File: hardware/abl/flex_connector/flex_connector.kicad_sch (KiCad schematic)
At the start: 2 parts, among them J1 Conn_01x20_Pin, J2 Conn_01x20_Pin

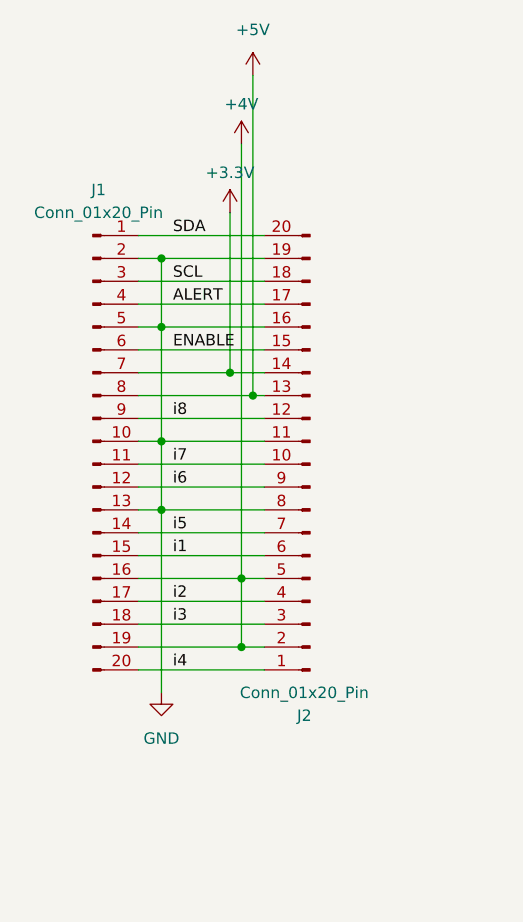
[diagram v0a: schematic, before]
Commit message: Rename files, names and labels to be more consistent. Add READMEs for connectors and extend some other READMEs.
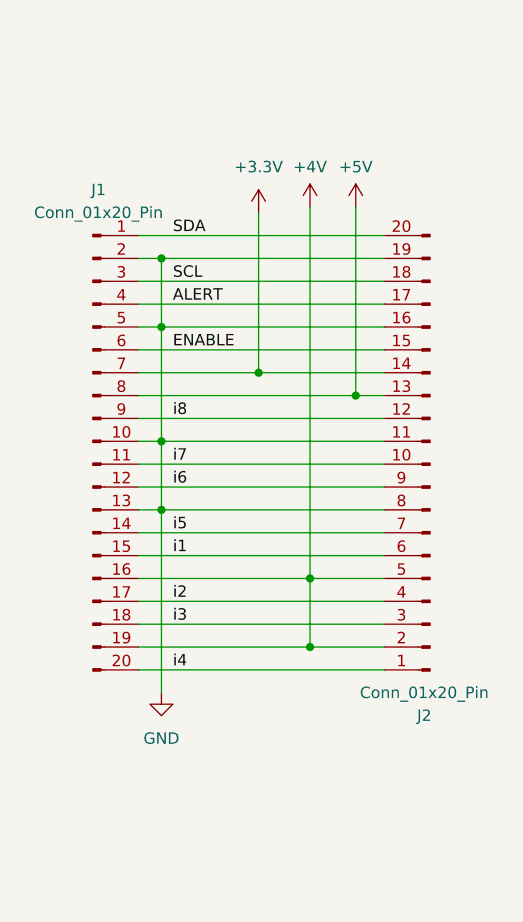
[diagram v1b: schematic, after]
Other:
- title: (none) -> besteLampe! ABL Flex Connector
- moved on the sheet: J2

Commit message: Add current renderings to all ABL PCBs.
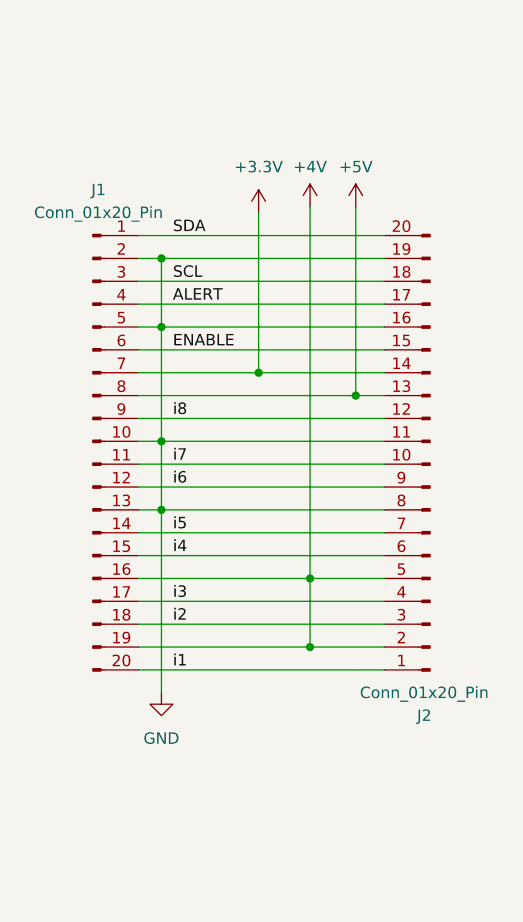
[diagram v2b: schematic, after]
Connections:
- net i1: now also J1.20 (Pin_20), J2.1 (Pin_1); no longer J1.15 (Pin_15), J2.6 (Pin_6)
- net i2: now also J1.18 (Pin_18), J2.3 (Pin_3); no longer J1.17 (Pin_17), J2.4 (Pin_4)
- net i3: now also J1.17 (Pin_17), J2.4 (Pin_4); no longer J1.18 (Pin_18), J2.3 (Pin_3)
- net i4: now also J1.15 (Pin_15), J2.6 (Pin_6); no longer J1.20 (Pin_20), J2.1 (Pin_1)
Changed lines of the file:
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@@
 	)
 	(label "i2"
-		(at 58.42 95.25 0)
+		(at 58.42 97.79 0)
 		(fields_autoplaced yes)
 		(effects
@@
 	)
 	(label "i3"
-		(at 58.42 97.79 0)
+		(at 58.42 95.25 0)
 		(fields_autoplaced yes)
 		(effects
@@
 	)
 	(label "i4"
-		(at 58.42 102.87 0)
+		(at 58.42 90.17 0)
 		(fields_autoplaced yes)
 		(effects
@@
 	)
 	(label "i1"
-		(at 58.42 90.17 0)
+		(at 58.42 102.87 0)
 		(fields_autoplaced yes)
 		(effects
@@
 		(on_board yes)
 		(dnp no)
-		(fields_autoplaced yes)
 		(property "Reference" "J1"
 			(at 50.165 49.53 0)

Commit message: Many small adjustments for the next production run.
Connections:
- net +5V is gone; now on net +4V: J1.8 (Pin_8), J2.13 (Pin_13)
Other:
- note added: "Pin numbering of this schematics / symbols contradicts that of the rigid PCBs, but the result should be all right."
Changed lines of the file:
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@@
 	(title_block
 		(title "besteLampe! ABL Flex Connector")
-		(date "2024-10-01")
-		(rev "1.0")
+		(date "2024-11-26")
+		(rev "1.1")
 		(comment 1 "See  https://lenaschimmel.de/besteLampe! for the source and more information")
 		(comment 2 "This source describes Open Hardware and is licensed under the CERN-OHL-S v2.")
@@
 	)
 	(junction
+		(at 73.66 46.355)
+		(diameter 0)
+		(color 0 0 0 0)
+	)
+	(junction
+		(at 78.74 46.355)
+		(diameter 0)
+		(color 0 0 0 0)
+	)
+	(junction
 		(at 67.945 69.85)
 		(diameter 0)
@@
 	(wire
 		(pts
-			(xy 78.74 51.435) (xy 78.74 72.39)
+			(xy 78.74 43.18) (xy 78.74 46.355)
+		)
+		(stroke
+			(width 0)
+			(type default)
+		)
+	)
+	(wire
+		(pts
+			(xy 78.74 46.355) (xy 78.74 72.39)
 		)
 		(stroke
@@
 	(wire
 		(pts
-			(xy 73.66 51.435) (xy 73.66 92.71)
+			(xy 73.66 43.18) (xy 73.66 46.355)
 		)
 		(stroke
@@
 	(wire
 		(pts
+			(xy 73.66 46.355) (xy 73.66 92.71)
+		)
+		(stroke
+			(width 0)
+			(type default)
+		)
+	)
+	(wire
+		(pts
 			(xy 67.945 69.85) (xy 81.915 69.85)
 		)
@@
 	(wire
 		(pts
+			(xy 73.66 46.355) (xy 78.74 46.355)
+		)
+		(stroke
+			(width 0)
+			(type default)
+		)
+	)
+	(wire
+		(pts
 			(xy 54.61 92.71) (xy 73.66 92.71)
 		)
@@
 			(width 0)
 			(type default)
+		)
+	)
+	(text "Pin numbering of this schematics / symbols\ncontradicts that of the rigid PCBs, but \nthe result should be all right."
+		(exclude_from_sim no)
+		(at 68.58 125.73 0)
+		(effects
+			(font
+				(size 1.27 1.27)
+			)
 		)
 	)
@@
 	(symbol
 		(lib_id "power:+5V")
-		(at 78.74 51.435 0)
+		(at 78.74 43.18 0)
 		(unit 1)
 		(exclude_from_sim no)
@@
 		(dnp no)
 		(property "Reference" "#PWR09"
-			(at 78.74 55.245 0)
+			(at 78.74 46.99 0)
 			(effects
 				(font
@@
 		)
 		(property "Value" "+5V"
-			(at 78.74 46.99 0)
+			(at 78.74 38.735 0)
 			(effects
 				(font
@@
 		)
 		(property "Footprint" ""
-			(at 78.74 51.435 0)
+			(at 78.74 43.18 0)
 			(effects
 				(font
@@
 		)
 		(property "Datasheet" ""
-			(at 78.74 51.435 0)
+			(at 78.74 43.18 0)
 			(effects
 				(font
@@
 		)
 		(property "Description" "Power symbol creates a global label with name \"+5V\""
-			(at 78.74 51.435 0)
+			(at 78.74 43.18 0)
 			(effects
 				(font
@@
 	(symbol
 		(lib_id "power:+4V")
-		(at 73.66 51.435 0)
+		(at 73.66 43.18 0)
 		(unit 1)
 		(exclude_from_sim no)
@@
 		(fields_autoplaced yes)
 		(property "Reference" "#PWR010"
-			(at 73.66 55.245 0)
+			(at 73.66 46.99 0)
 			(effects
 				(font
@@
 		)
 		(property "Value" "+4V"
-			(at 73.66 46.99 0)
+			(at 73.66 38.735 0)
 			(effects
 				(font
@@
 		)
 		(property "Footprint" ""
-			(at 73.66 51.435 0)
+			(at 73.66 43.18 0)
 			(effects
 				(font
@@
 		)
 		(property "Datasheet" ""
-			(at 73.66 51.435 0)
+			(at 73.66 43.18 0)
 			(effects
 				(font
@@
 		)
 		(property "Description" "Power symbol creates a global label with name \"+4V\""
-			(at 73.66 51.435 0)
-			(effects
-				(font
+			(at 73.66 43.18 0)
+			(effects
+				(font
